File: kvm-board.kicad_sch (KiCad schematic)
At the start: 19 parts, among them J1 TYPE-C-31-M-12, J2 TYPE-C-31-M-12, U1 CH9329, U2 CH340N

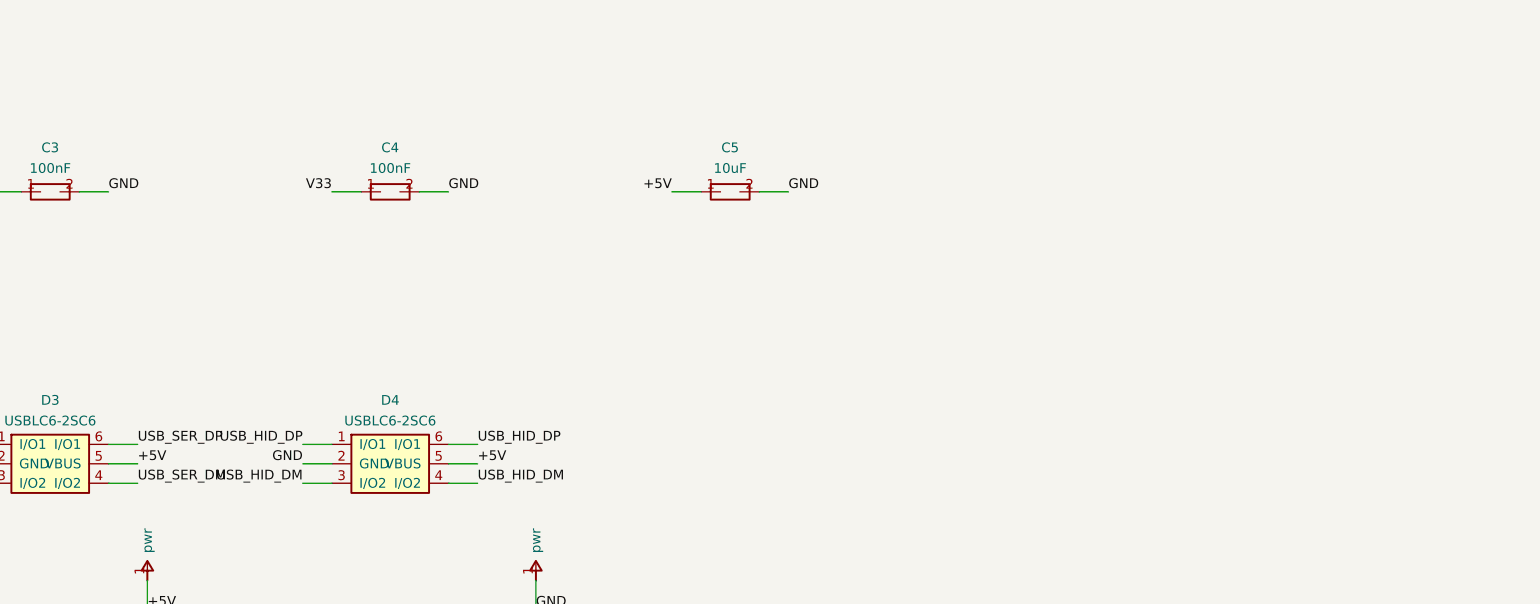
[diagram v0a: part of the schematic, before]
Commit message: Fix ESD clamp rails and add local VBUS decoupling
Connect the USBLC6 VBUS pins to each port's local VBUS instead of the
common +5V rail, and add 100 nF at each ESD array as recommended by the
ST datasheet. Add a pin-level review document.

Verified: ERC 0, DRC 0, schematic/PCB netlists match.
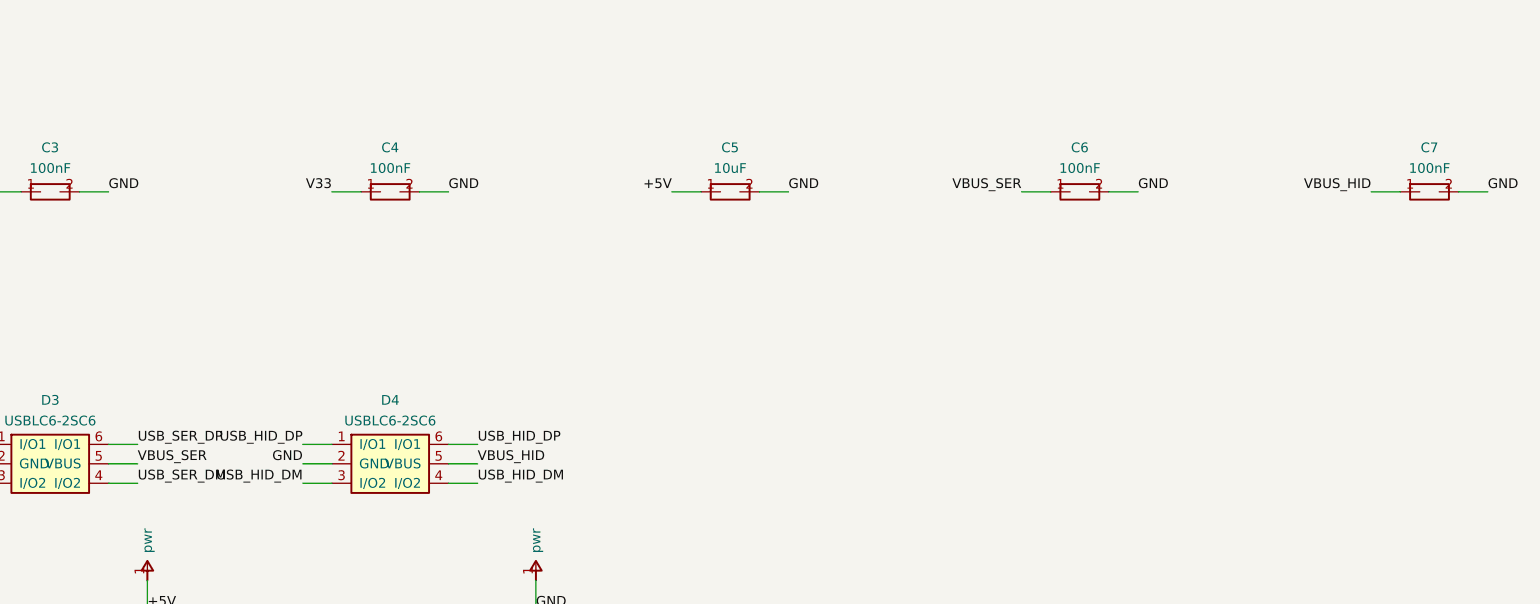
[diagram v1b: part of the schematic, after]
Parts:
- added C6, C7: 100nF, KVM:C_0603_1608Metric, symbol kvm:C
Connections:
- net +5V: no longer D3.5 (VBUS), D4.5 (VBUS)
- net GND: now also C6.2, C7.2
- net VBUS_HID: now also D4.5 (VBUS), C7.1
- net VBUS_SER: now also D3.5 (VBUS), C6.1
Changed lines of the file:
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@@
   (label "USB_SER_DP" (at 151.13 236.22 0) (effects (font (size 1.27 1.27)) (justify left bottom)))
   (wire (pts (xy 147.32 238.76) (xy 151.13 238.76)) (stroke (width 0) (type default)))
-  (label "+5V" (at 151.13 238.76 0) (effects (font (size 1.27 1.27)) (justify left bottom)))
+  (label "VBUS_SER" (at 151.13 238.76 0) (effects (font (size 1.27 1.27)) (justify left bottom)))
   (wire (pts (xy 147.32 241.3) (xy 151.13 241.3)) (stroke (width 0) (type default)))
   (label "USB_SER_DM" (at 151.13 241.3 0) (effects (font (size 1.27 1.27)) (justify left bottom)))
@@
   (label "USB_HID_DP" (at 195.58 236.22 0) (effects (font (size 1.27 1.27)) (justify left bottom)))
   (wire (pts (xy 191.77 238.76) (xy 195.58 238.76)) (stroke (width 0) (type default)))
-  (label "+5V" (at 195.58 238.76 0) (effects (font (size 1.27 1.27)) (justify left bottom)))
+  (label "VBUS_HID" (at 195.58 238.76 0) (effects (font (size 1.27 1.27)) (justify left bottom)))
   (wire (pts (xy 191.77 241.3) (xy 195.58 241.3)) (stroke (width 0) (type default)))
   (label "USB_HID_DM" (at 195.58 241.3 0) (effects (font (size 1.27 1.27)) (justify left bottom)))
@@
   (wire (pts (xy 232.41 203.2) (xy 236.22 203.2)) (stroke (width 0) (type default)))
   (label "GND" (at 236.22 203.2 0) (effects (font (size 1.27 1.27)) (justify left bottom)))
+  (symbol (lib_id "kvm:C") (at 274.32 203.2 0) (unit 1)
+    (exclude_from_sim no) (in_bom yes) (on_board yes) (dnp no)
+    (property "Reference" "C6" (at 274.32 197.43 0) (effects (font (size 1.27 1.27))))
+    (property "Value" "100nF" (at 274.32 200.13 0) (effects (font (size 1.27 1.27))))
+    (property "Footprint" "KVM:C_0603_1608Metric" (at 274.32 203.2 0) (effects (font (size 1.27 1.27)) hide))
+    (property "Datasheet" "" (at 274.32 203.2 0) (effects (font (size 1.27 1.27)) hide))
+    (property "LCSC" "C14663" (at 274.32 203.2 0) (effects (font (size 1.27 1.27)) hide))
+    (pin "1")
+    (pin "2")
+    (instances (project "kvm-board" (path "/0e6e9d0a-6a7b-4f4e-9d3a-6f3f5c2b1a01" (reference "C6") (unit 1))))
+  )
+  (wire (pts (xy 270.51 203.2) (xy 266.7 203.2)) (stroke (width 0) (type default)))
+  (label "VBUS_SER" (at 266.7 203.2 0) (effects (font (size 1.27 1.27)) (justify right bottom)))
+  (wire (pts (xy 278.13 203.2) (xy 281.94 203.2)) (stroke (width 0) (type default)))
+  (label "GND" (at 281.94 203.2 0) (effects (font (size 1.27 1.27)) (justify left bottom)))
+  (symbol (lib_id "kvm:C") (at 320.04 203.2 0) (unit 1)
+    (exclude_from_sim no) (in_bom yes) (on_board yes) (dnp no)
+    (property "Reference" "C7" (at 320.04 197.43 0) (effects (font (size 1.27 1.27))))
+    (property "Value" "100nF" (at 320.04 200.13 0) (effects (font (size 1.27 1.27))))
+    (property "Footprint" "KVM:C_0603_1608Metric" (at 320.04 203.2 0) (effects (font (size 1.27 1.27)) hide))
+    (property "Datasheet" "" (at 320.04 203.2 0) (effects (font (size 1.27 1.27)) hide))
+    (property "LCSC" "C14663" (at 320.04 203.2 0) (effects (font (size 1.27 1.27)) hide))
+    (pin "1")
+    (pin "2")
+    (instances (project "kvm-board" (path "/0e6e9d0a-6a7b-4f4e-9d3a-6f3f5c2b1a01" (reference "C7") (unit 1))))
+  )
+  (wire (pts (xy 316.23 203.2) (xy 312.42 203.2)) (stroke (width 0) (type default)))
+  (label "VBUS_HID" (at 312.42 203.2 0) (effects (font (size 1.27 1.27)) (justify right bottom)))
+  (wire (pts (xy 323.85 203.2) (xy 327.66 203.2)) (stroke (width 0) (type default)))
+  (label "GND" (at 327.66 203.2 0) (effects (font (size 1.27 1.27)) (justify left bottom)))
   (symbol (lib_id "kvm:PWR_FLAG") (at 152.4 254 0) (unit 1)
     (exclude_from_sim no) (in_bom no) (on_board no) (dnp no)

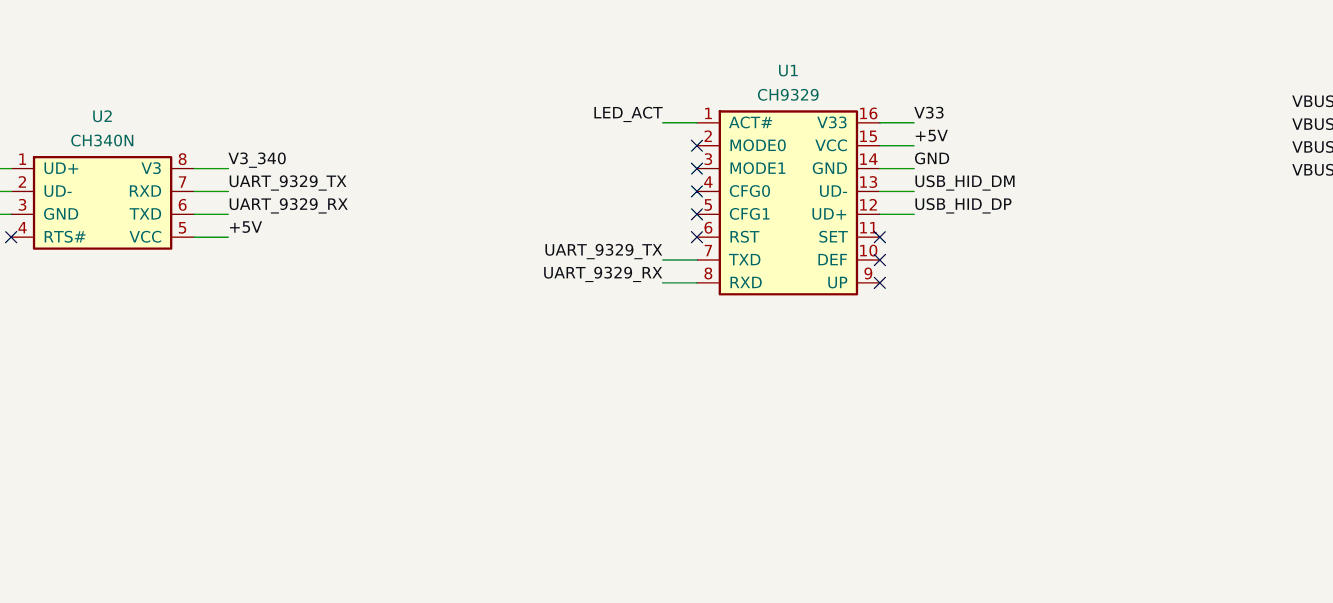
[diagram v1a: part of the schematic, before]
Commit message: Document UART crossover and strap-pin defaults on the schematic
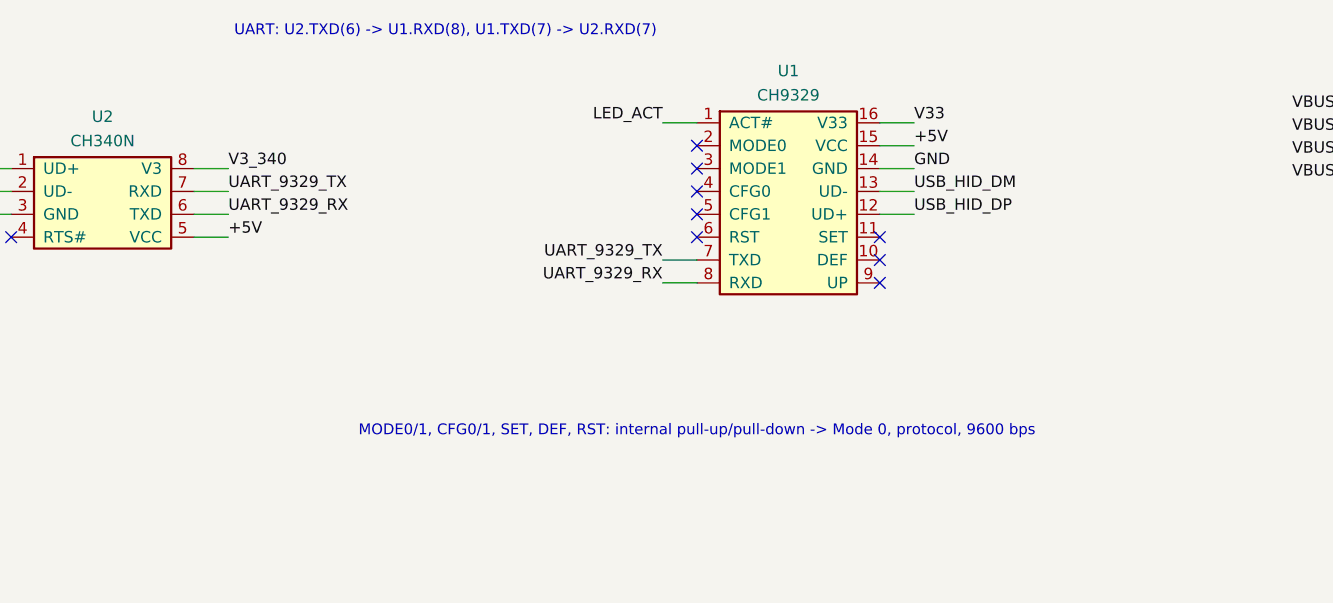
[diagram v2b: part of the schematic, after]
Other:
- note added: "MODE0/1, CFG0/1, SET, DEF, RST: internal pull-up/pull-down -> Mode 0, protocol, 9600 bps"
- note added: "UART: U2.TXD(6) -> U1.RXD(8), U1.TXD(7) -> U2.RXD(7)"
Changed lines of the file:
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@@
     (comment 2 "Fits a Frisk mint tin: 56 x 27 mm")
   )
+  (text "UART: U2.TXD(6) -> U1.RXD(8), U1.TXD(7) -> U2.RXD(7)" (at 177.8 69.85 0) (effects (font (size 1.2 1.2))))
+  (text "MODE0/1, CFG0/1, SET, DEF, RST: internal pull-up/pull-down -> Mode 0, protocol, 9600 bps" (at 205.74 114.3 0) (effects (font (size 1.2 1.2))))
   (symbol (lib_id "kvm:USB_C") (at 76.2 88.9 0) (unit 1)
     (exclude_from_sim no) (in_bom yes) (on_board yes) (dnp no)

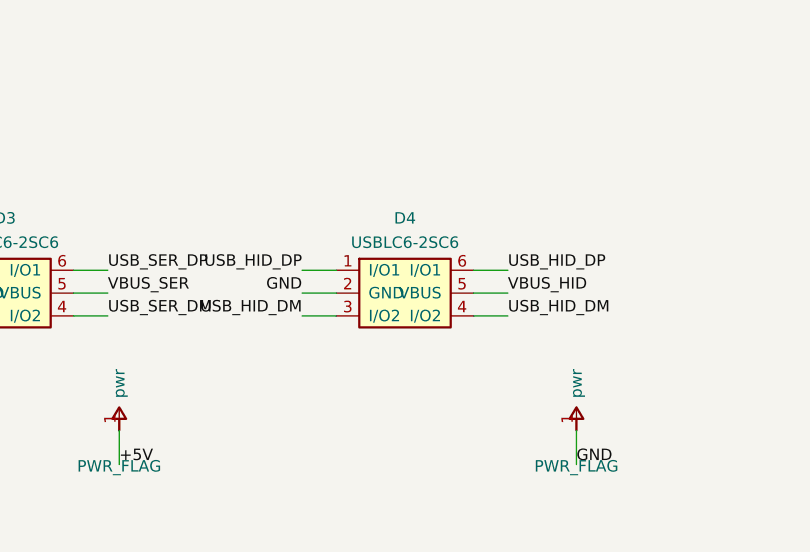
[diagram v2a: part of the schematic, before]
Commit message: Fit the board outline to the published FRISK-CASE 3D model
Reshape the PCB to 65.4 x 31.4 mm with a 6.8 x 19.8 mm latch notch measured from the published FRISK_CASE1.stl, move J2 to the upper-right lobe, and swap D4's two identical USBLC6 channels so the J2 fanout stays planar. Regenerate the schematic, board images, gerbers, CPL and position files. DRC and ERC are clean.
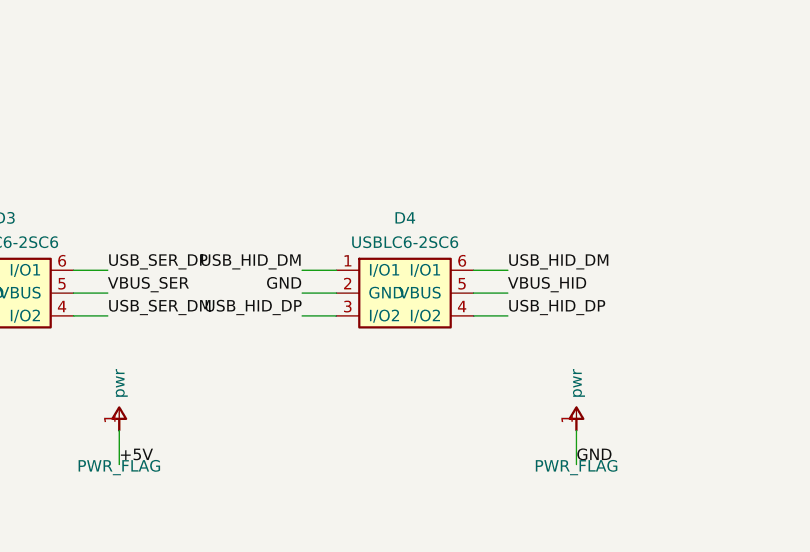
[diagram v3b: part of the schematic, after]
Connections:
- net USB_HID_DM: now also D4.1 (I/O1), D4.6 (I/O1); no longer D4.3 (I/O2), D4.4 (I/O2)
- net USB_HID_DP: now also D4.3 (I/O2), D4.4 (I/O2); no longer D4.1 (I/O1), D4.6 (I/O1)
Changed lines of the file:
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@@
     (rev "A")
     (comment 1 "UART(USB serial) to USB HID keyboard/mouse")
-    (comment 2 "Fits a Frisk mint tin: 56 x 27 mm")
+    (comment 2 "Fits the published FRISK-CASE 3D model: 65.4 x 31.4 mm")
   )
   (text "UART: U2.TXD(6) -> U1.RXD(8), U1.TXD(7) -> U2.RXD(7)" (at 177.8 69.85 0) (effects (font (size 1.2 1.2))))
@@
   )
   (wire (pts (xy 176.53 236.22) (xy 172.72 236.22)) (stroke (width 0) (type default)))
-  (label "USB_HID_DP" (at 172.72 236.22 0) (effects (font (size 1.27 1.27)) (justify right bottom)))
+  (label "USB_HID_DM" (at 172.72 236.22 0) (effects (font (size 1.27 1.27)) (justify right bottom)))
   (wire (pts (xy 176.53 238.76) (xy 172.72 238.76)) (stroke (width 0) (type default)))
   (label "GND" (at 172.72 238.76 0) (effects (font (size 1.27 1.27)) (justify right bottom)))
   (wire (pts (xy 176.53 241.3) (xy 172.72 241.3)) (stroke (width 0) (type default)))
-  (label "USB_HID_DM" (at 172.72 241.3 0) (effects (font (size 1.27 1.27)) (justify right bottom)))
+  (label "USB_HID_DP" (at 172.72 241.3 0) (effects (font (size 1.27 1.27)) (justify right bottom)))
   (wire (pts (xy 191.77 236.22) (xy 195.58 236.22)) (stroke (width 0) (type default)))
-  (label "USB_HID_DP" (at 195.58 236.22 0) (effects (font (size 1.27 1.27)) (justify left bottom)))
+  (label "USB_HID_DM" (at 195.58 236.22 0) (effects (font (size 1.27 1.27)) (justify left bottom)))
   (wire (pts (xy 191.77 238.76) (xy 195.58 238.76)) (stroke (width 0) (type default)))
   (label "VBUS_HID" (at 195.58 238.76 0) (effects (font (size 1.27 1.27)) (justify left bottom)))
   (wire (pts (xy 191.77 241.3) (xy 195.58 241.3)) (stroke (width 0) (type default)))
-  (label "USB_HID_DM" (at 195.58 241.3 0) (effects (font (size 1.27 1.27)) (justify left bottom)))
+  (label "USB_HID_DP" (at 195.58 241.3 0) (effects (font (size 1.27 1.27)) (justify left bottom)))
   (symbol (lib_id "kvm:R") (at 50.8 170.18 0) (unit 1)
     (exclude_from_sim no) (in_bom yes) (on_board yes) (dnp no)
